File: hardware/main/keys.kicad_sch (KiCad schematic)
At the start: 134 parts, among them SW1 Esc, SW10 a, SW12 Fn, SW13 F2, SW14 2, SW15 w, SW16 s, SW17 z, SW18 Tux, SW19 F3, SW2 F1, SW20 3, SW21 e, SW22 d, SW23 c, SW24 Alt, SW25 F4, SW26 4, SW27 r, SW28 f, SW29 v, SW3 tilde, SW31 F5, SW32 5, SW33 t, SW34 g, SW35 b, SW36 F6, SW37 6, SW38 y, SW39 h, SW4 Tab, SW40 n, SW41 F7, SW42 7, SW43 u, SW44 j, SW45 m, SW46 Space, SW47 F8, SW48 8, SW49 i, SW5 Caps Lock, SW50 k, SW51 comma, SW52 F9, SW53 9, SW54 o, SW55 l, SW56 dot, SW57 F10, SW58 0, SW59 p, SW6 Shift, SW60 semicolon, SW61 slash, SW62 Alt Gr, SW63 F11, SW64 minus, SW65 sq br open, SW66 apostrophe, SW67 Menu, SW68 F12, SW69 equal, SW7 Ctrl, SW70 sq br close, SW71 backslash, SW72 Shift, SW73 Ctrl, SW74 Print, SW75 Backspace, SW76 Enter, SW77 Left, SW78 Scroll Lock, SW79 Up, SW8 1, SW80 Down, SW81 Pause, SW82 INS, SW83 DEL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

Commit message: Add circuit to disconnect the shift registers
This is done to save energy when the keyboard is switched off.
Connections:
- net VCC_SW renamed VCC_KEYS
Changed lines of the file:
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@@
 (kicad_sch (version 20210123) (generator eeschema)
   (paper "A3")
-  (junction (at 27.94 58.42) (diameter 1.016) (color 0 0 0 0))
+  (junction (at 26.67 58.42) (diameter 1.016) (color 0 0 0 0))
   (junction (at 58.42 40.64) (diameter 1.016) (color 0 0 0 0))
   (junction (at 96.52 30.48) (diameter 1.016) (color 0 0 0 0))
@@
   (no_connect (at 269.24 208.28))
   (no_connect (at 317.5 137.16))
-  (wire (pts (xy 25.4 58.42) (xy 27.94 58.42))
-    (stroke (width 0) (type solid) (color 0 0 0 0))
-  )
-  (wire (pts (xy 27.94 58.42) (xy 27.94 66.04))
-    (stroke (width 0) (type solid) (color 0 0 0 0))
-  )
-  (wire (pts (xy 27.94 58.42) (xy 40.64 58.42))
+  (wire (pts (xy 24.13 58.42) (xy 26.67 58.42))
+    (stroke (width 0) (type solid) (color 0 0 0 0))
+  )
+  (wire (pts (xy 26.67 58.42) (xy 26.67 66.04))
+    (stroke (width 0) (type solid) (color 0 0 0 0))
+  )
+  (wire (pts (xy 26.67 58.42) (xy 40.64 58.42))
     (stroke (width 0) (type solid) (color 0 0 0 0))
   )
@@
     (stroke (width 0) (type solid) (color 0 0 0 0))
   )
+  (wire (pts (xy 38.1 68.58) (xy 38.1 71.12))
+    (stroke (width 0) (type solid) (color 0 0 0 0))
+  )
   (wire (pts (xy 38.1 68.58) (xy 40.64 68.58))
     (stroke (width 0) (type solid) (color 0 0 0 0))
   )
-  (wire (pts (xy 40.64 66.04) (xy 27.94 66.04))
-    (stroke (width 0) (type solid) (color 0 0 0 0))
-  )
-  (wire (pts (xy 50.8 48.26) (xy 58.42 48.26))
+  (wire (pts (xy 40.64 66.04) (xy 26.67 66.04))
+    (stroke (width 0) (type solid) (color 0 0 0 0))
+  )
+  (wire (pts (xy 50.8 46.99) (xy 50.8 48.26))
+    (stroke (width 0) (type solid) (color 0 0 0 0))
+  )
+  (wire (pts (xy 50.8 46.99) (xy 58.42 46.99))
     (stroke (width 0) (type solid) (color 0 0 0 0))
   )
@@
     (stroke (width 0) (type solid) (color 0 0 0 0))
   )
-  (wire (pts (xy 58.42 40.64) (xy 58.42 48.26))
+  (wire (pts (xy 58.42 40.64) (xy 58.42 46.99))
     (stroke (width 0) (type solid) (color 0 0 0 0))
   )
@@
     (effects (font (size 1.27 1.27)) (justify left bottom))
   )
-  (hierarchical_label "SPI_SCK" (shape input) (at 25.4 58.42 180)
+  (hierarchical_label "SPI_SCK" (shape input) (at 24.13 58.42 180)
     (effects (font (size 1.27 1.27)) (justify right))
   )
@@
     (effects (font (size 1.27 1.27)) (justify right))
   )
-  (hierarchical_label "VCC_SW" (shape input) (at 38.1 60.96 180)
+  (hierarchical_label "VCC_KEYS" (shape input) (at 38.1 60.96 180)
     (effects (font (size 1.27 1.27)) (justify right))
   )
-  (hierarchical_label "VCC_SW" (shape input) (at 58.42 38.1 90)
+  (hierarchical_label "VCC_KEYS" (shape input) (at 58.42 38.1 90)
     (effects (font (size 1.27 1.27)) (justify left))
   )
@@
     (effects (font (size 1.27 1.27)) (justify right))
   )
-  (hierarchical_label "VCC_SW" (shape input) (at 137.16 218.44 90)
+  (hierarchical_label "VCC_KEYS" (shape input) (at 137.16 218.44 90)
     (effects (font (size 1.27 1.27)) (justify left))
   )
@@
     (effects (font (size 1.27 1.27)) (justify left))
   )
-  (hierarchical_label "VCC_SW" (shape input) (at 279.4 218.44 90)
+  (hierarchical_label "VCC_KEYS" (shape input) (at 279.4 218.44 90)
     (effects (font (size 1.27 1.27)) (justify left))
   )
-  (symbol (lib_id "power:GND") (at 38.1 68.58 0) (unit 1)
+  (symbol (lib_id "power:GND") (at 38.1 71.12 0) (unit 1)
     (in_bom yes) (on_board yes)
-    (property "Reference" "#PWR0111" (id 0) (at 38.1 74.93 0)
+    (property "Reference" "#PWR0111" (id 0) (at 38.1 77.47 0)
       (effects (font (size 1.27 1.27)) hide)
     )
-    (property "Value" "GND" (id 1) (at 39.37 73.66 0))
-    (property "Footprint" "" (id 2) (at 38.1 68.58 0)
+    (property "Value" "GND" (id 1) (at 39.37 76.2 0))
+    (property "Footprint" "" (id 2) (at 38.1 71.12 0)
       (effects (font (size 1.27 1.27)) hide)
     )
-    (property "Datasheet" "" (id 3) (at 38.1 68.58 0)
+    (property "Datasheet" "" (id 3) (at 38.1 71.12 0)
       (effects (font (size 1.27 1.27)) hide)
     )

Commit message: Add the USB sense circuit to the PCB
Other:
- note added: "TODO: pull-ups for each column"
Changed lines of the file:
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@@
+    (effects (font (size 1.27 1.27)) (justify left bottom))
+  )
+  (text "TODO:\npull-ups for each column" (at 97.79 255.27 0)
     (effects (font (size 1.27 1.27)) (justify left bottom))
   )

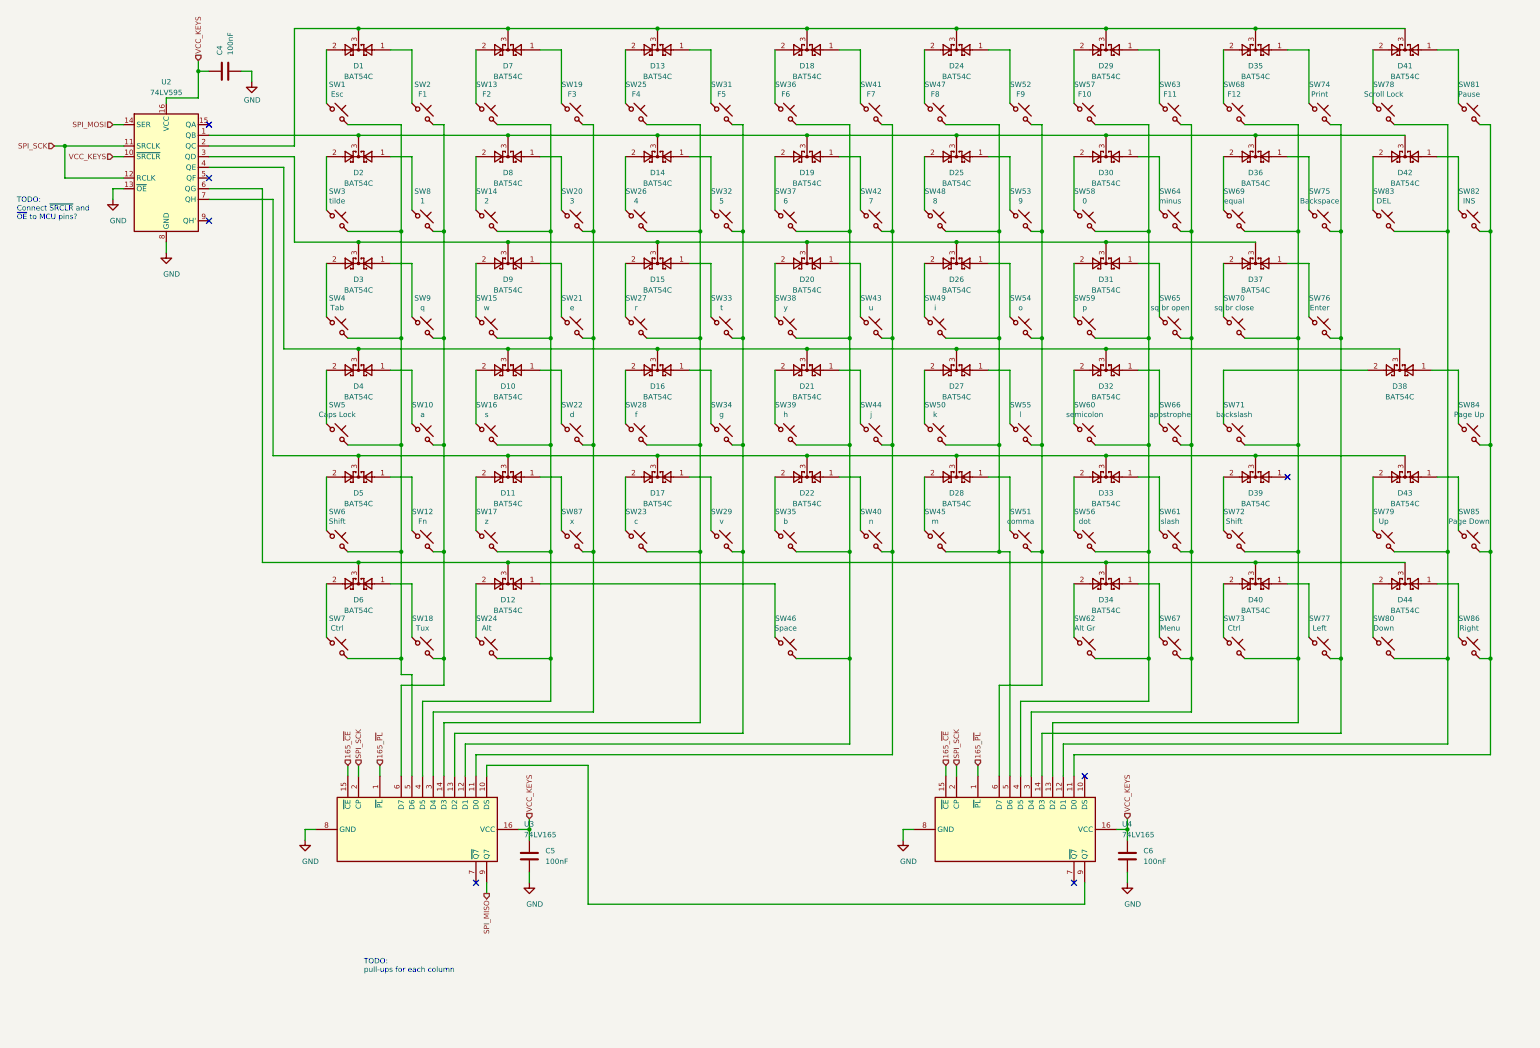
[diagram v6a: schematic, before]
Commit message: Add pull-up resistors to the key matrix
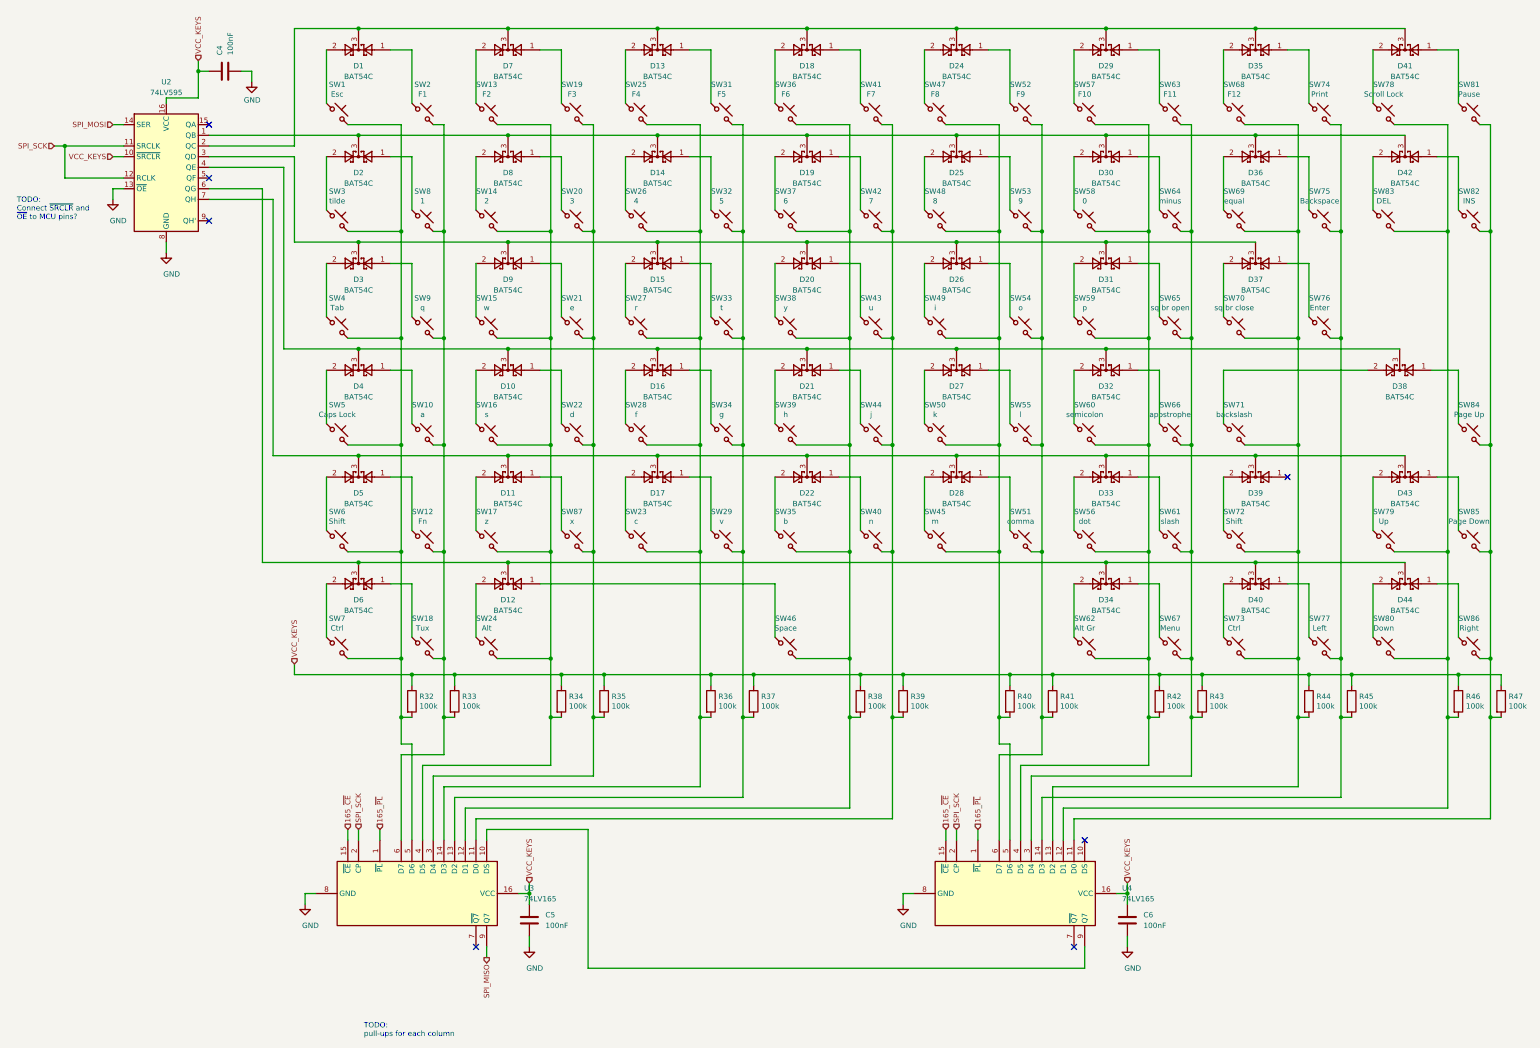
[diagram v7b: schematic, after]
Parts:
- added R32, R33, R34, R35, R36, R37, R38, R39, R40, R41, R42, R43, R44, R45, R46, R47: 100k, Resistor_SMD:R_0603_1608Metric_Pad0.98x0.95mm_HandSolder, symbol Device:R
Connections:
- net VCC_KEYS: now also R32.1, R33.1, R34.1, R35.1, R36.1, R37.1, R38.1, R39.1, R40.1, R41.1, R42.1, R43.1, R44.1, R45.1, R46.1, R47.1
- net at SW1.2, SW3.2, SW4.2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: now also R32.2
- net at SW10.2, SW12.2, SW18.2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: now also R33.2
- net at SW40.2, SW41.2, SW42.2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: now also R39.2
- net at SW81.2, SW82.2, SW84.2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: now also R47.2
- net at SW61.2, SW63.2, SW64.2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: now also R43.2
- net at SW56.2, SW57.2, SW58.2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: now also R42.2
- net at SW78.2, SW79.2, SW80.2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: now also R46.2
- net at SW68.2, SW69.2, SW70.2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: now also R44.2
- net at SW19.2, SW20.2, SW21.2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: now also R35.2
- net at SW13.2, SW14.2, SW15.2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: now also R34.2
- net at SW45.2, SW47.2, SW48.2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: now also R40.2
- net at SW35.2, SW36.2, SW37.2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: now also R38.2
- net at SW51.2, SW52.2, SW53.2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: now also R41.2
- net at SW29.2, SW31.2, SW32.2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: now also R37.2
- net at SW23.2, SW25.2, SW26.2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: now also R36.2
- net at SW74.2, SW75.2, SW76.2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: now also R45.2
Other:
- moved on the sheet: C5, C6, U3, U4
